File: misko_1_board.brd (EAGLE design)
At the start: 115 x 115 mm, 151 parts, among them IC1 ATMEGA1281-16AU, IC10 ORG1510-MK4, IC11 TPS3808G33DBVT, IC12 LTC4425, IC13 RN4678_BT_MODULE, IC14 ADXL345, IC15 74HCT1G32, IC16 FM25W256-SOIC, IC17 MICROSD_SPI_MODE, IC18 FH12-30S-0.5SH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

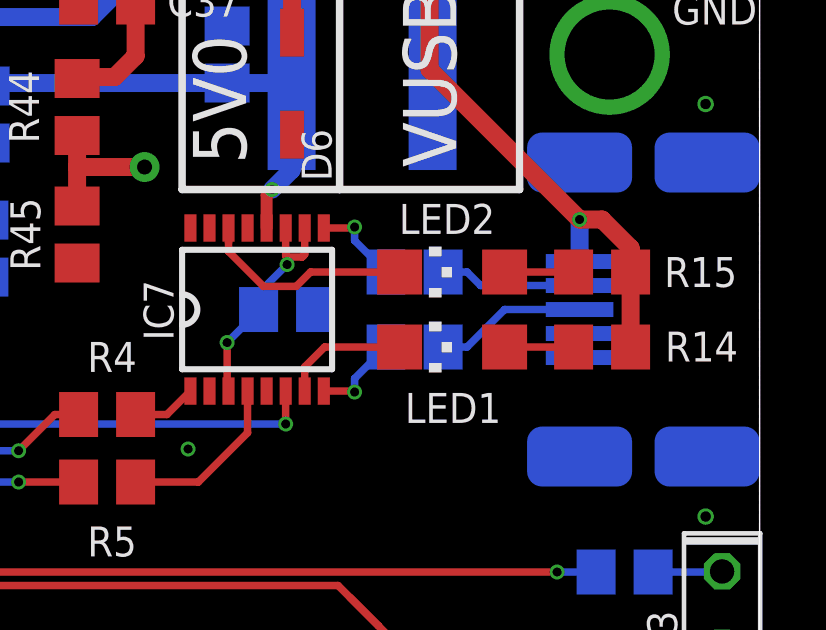
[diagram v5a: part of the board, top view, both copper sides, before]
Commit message: - named FTDI RX/TX LEDs properly in schematic and on board layout (tplace)
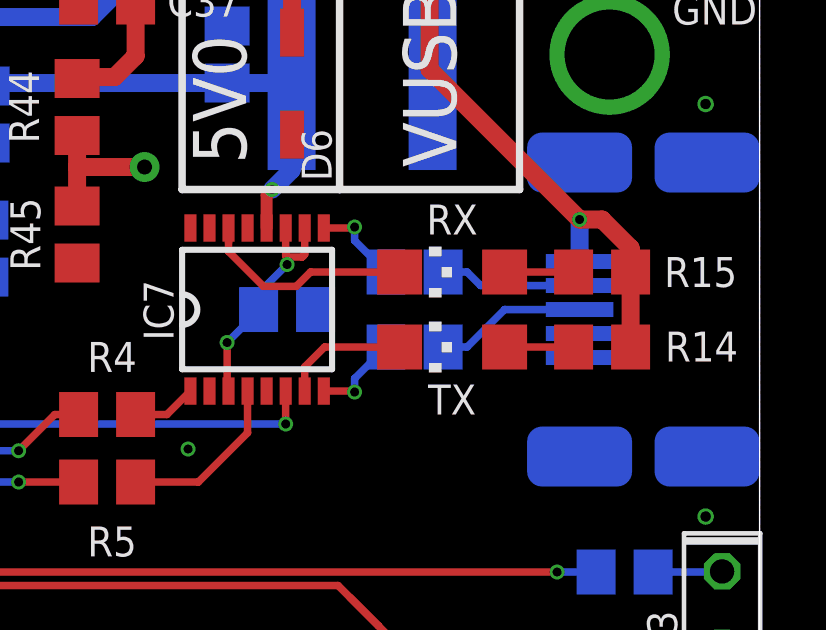
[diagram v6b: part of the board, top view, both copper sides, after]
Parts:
- LED1: value yellow -> TX
- LED2: value yellow -> RX
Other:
- board text added: "RX"
- board text added: "TX"
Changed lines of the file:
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@@
 <text x="97" y="66.5" size="1.778" layer="21" font="vector" rot="R90" align="center">5V0</text>
 <text x="93.5" y="61" size="1.778" layer="22" font="vector" rot="MR270" align="center">LiPo</text>
+<text x="104.75" y="62.5" size="1" layer="21" font="vector" align="center">RX</text>
+<text x="104.75" y="56.5" size="1" layer="21" font="vector" align="center">TX</text>
 </plain>
 <attributes>
@@
 <attribute name="VALUE" x="111.337" y="46.79" size="1.016" layer="27" ratio="10" rot="R270"/>
 </element>
-<element name="LED1" library="led" library_urn="urn:adsk.eagle:library:259" package="CHIPLED_1206" value="yellow" x="104.75" y="58.25" smashed="yes" rot="R90">
-<attribute name="NAME" x="104.78" y="56.22" size="1" layer="25" font="vector" align="center"/>
+<element name="LED1" library="led" library_urn="urn:adsk.eagle:library:259" package="CHIPLED_1206" value="TX" x="104.75" y="58.25" smashed="yes" rot="R90">
 <attribute name="VALUE" x="106.02" y="60.79" size="1.27" layer="27" rot="R180"/>
 </element>
-<element name="LED2" library="led" library_urn="urn:adsk.eagle:library:259" package="CHIPLED_1206" value="yellow" x="104.75" y="60.75" smashed="yes" rot="R90">
-<attribute name="NAME" x="104.58" y="62.52" size="1" layer="25" font="vector" align="center"/>
+<element name="LED2" library="led" library_urn="urn:adsk.eagle:library:259" package="CHIPLED_1206" value="RX" x="104.75" y="60.75" smashed="yes" rot="R90">
 <attribute name="VALUE" x="106.02" y="63.29" size="1.27" layer="27" rot="R180"/>
 </element>

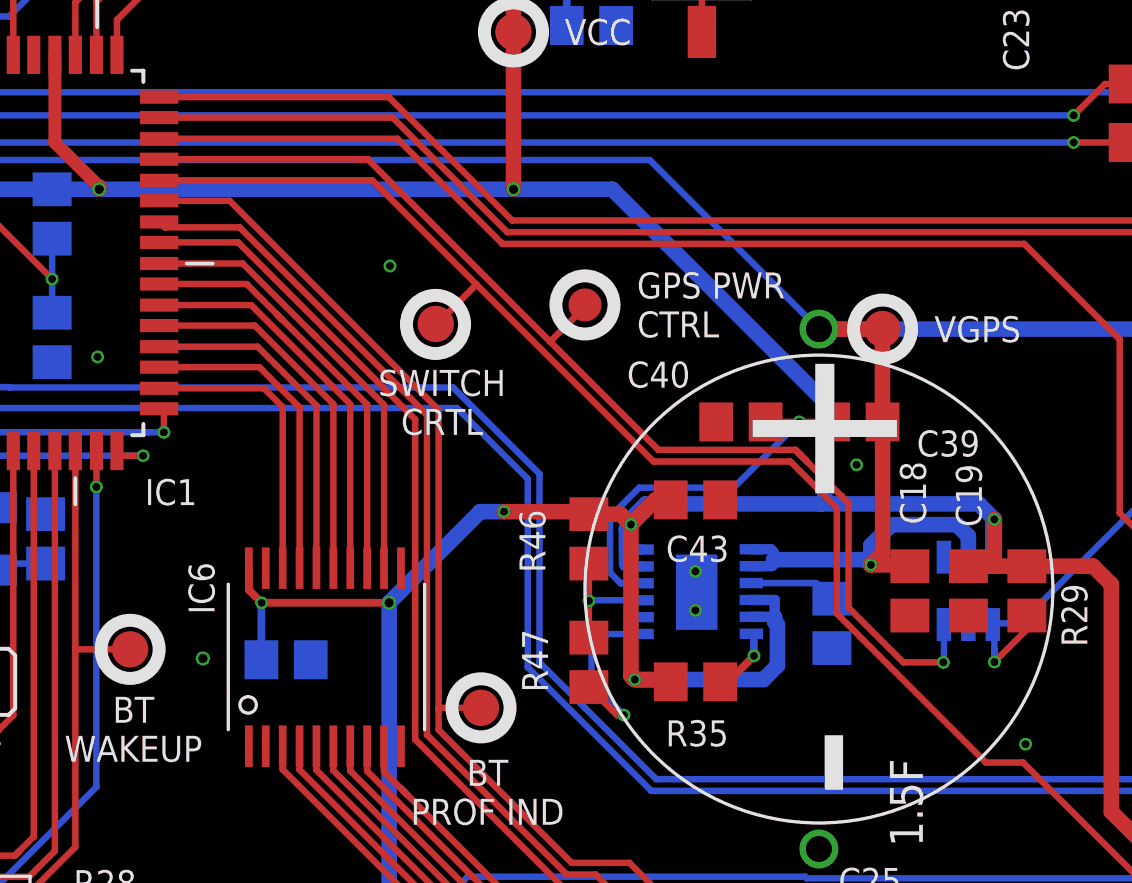
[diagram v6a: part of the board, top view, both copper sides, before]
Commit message: - added pulldown (R23) to GPS_POWER_CTL_PIN so that the receiver is turned off when micro controller resets
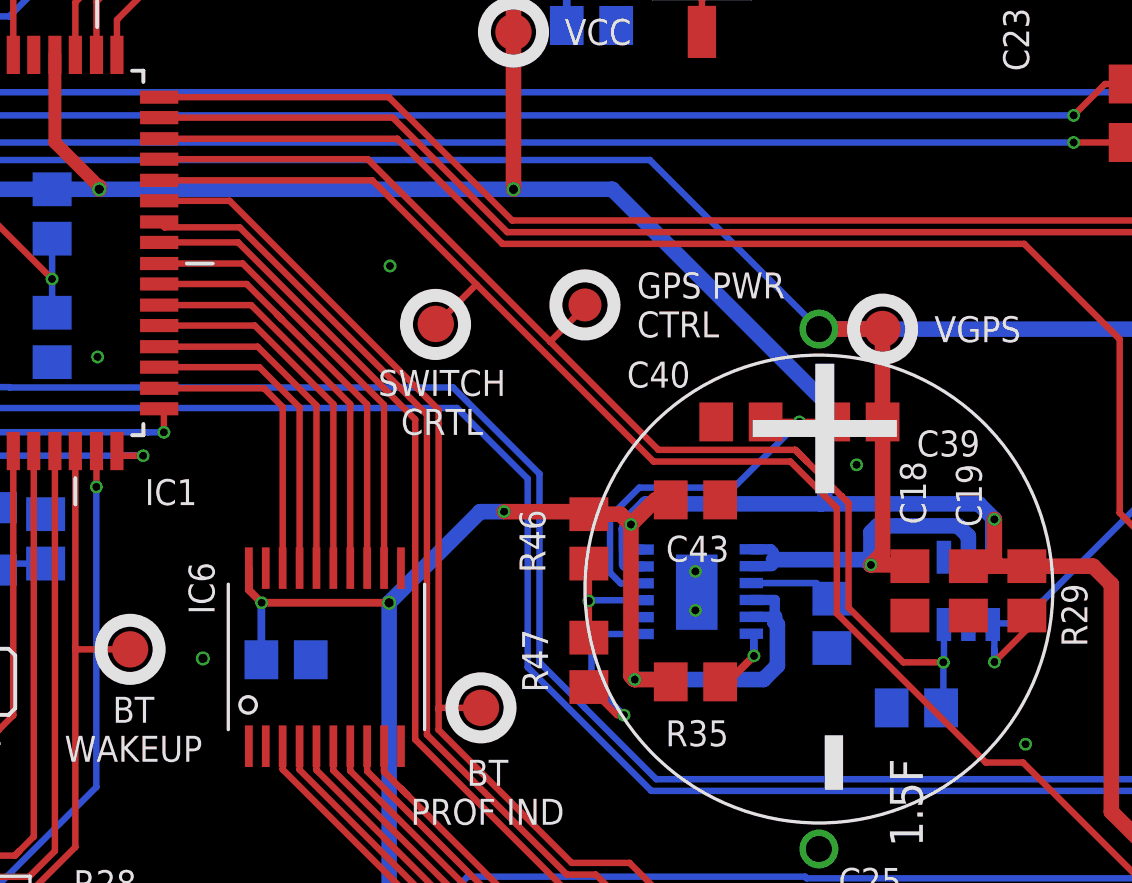
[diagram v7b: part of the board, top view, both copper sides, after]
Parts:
- added R23: 10k, resistor:R0805
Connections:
- net GND: now also R23.2
- net GPS_POWER_CTL_PIN: now also R23.1
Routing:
- net GPS_POWER_CTL_PIN: track 45.0 -> 46.4 mm
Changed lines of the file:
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@@
 <grid distance="0.25" unitdist="mm" unit="mm" style="lines" multiple="1" display="yes" altdistance="0.005" altunitdist="mm" altunit="mm"/>
 <layers>
-<layer number="1" name="Top" color="4" fill="1" visible="yes" active="yes"/>
+<layer number="1" name="Top" color="4" fill="1" visible="no" active="yes"/>
 <layer number="2" name="Route2" color="1" fill="3" visible="no" active="no"/>
 <layer number="3" name="Route3" color="4" fill="3" visible="no" active="no"/>
@@
 <layer number="14" name="Route14" color="1" fill="6" visible="no" active="no"/>
 <layer number="15" name="Route15" color="4" fill="6" visible="no" active="no"/>
-<layer number="16" name="Bottom" color="1" fill="1" visible="no" active="yes"/>
+<layer number="16" name="Bottom" color="1" fill="1" visible="yes" active="yes"/>
 <layer number="17" name="Pads" color="2" fill="1" visible="yes" active="yes"/>
 <layer number="18" name="Vias" color="2" fill="1" visible="yes" active="yes"/>
 <layer number="19" name="Unrouted" color="6" fill="1" visible="yes" active="yes"/>
 <layer number="20" name="Dimension" color="15" fill="1" visible="yes" active="yes"/>
-<layer number="21" name="tPlace" color="7" fill="1" visible="yes" active="yes"/>
-<layer number="22" name="bPlace" color="7" fill="1" visible="no" active="yes"/>
-<layer number="23" name="tOrigins" color="15" fill="1" visible="yes" active="yes"/>
-<layer number="24" name="bOrigins" color="15" fill="1" visible="no" active="yes"/>
-<layer number="25" name="tNames" color="7" fill="1" visible="yes" active="yes"/>
-<layer number="26" name="bNames" color="7" fill="1" visible="no" active="yes"/>
+<layer number="21" name="tPlace" color="7" fill="1" visible="no" active="yes"/>
+<layer number="22" name="bPlace" color="7" fill="1" visible="yes" active="yes"/>
+<layer number="23" name="tOrigins" color="15" fill="1" visible="no" active="yes"/>
+<layer number="24" name="bOrigins" color="15" fill="1" visible="yes" active="yes"/>
+<layer number="25" name="tNames" color="7" fill="1" visible="no" active="yes"/>
+<layer number="26" name="bNames" color="7" fill="1" visible="yes" active="yes"/>
 <layer number="27" name="tValues" color="7" fill="1" visible="no" active="yes"/>
 <layer number="28" name="bValues" color="7" fill="1" visible="no" active="yes"/>
@@
 <layer number="37" name="tTest" color="7" fill="1" visible="no" active="yes"/>
 <layer number="38" name="bTest" color="7" fill="1" visible="no" active="yes"/>
-<layer number="39" name="tKeepout" color="4" fill="11" visible="yes" active="yes"/>
-<layer number="40" name="bKeepout" color="1" fill="11" visible="no" active="yes"/>
-<layer number="41" name="tRestrict" color="4" fill="10" visible="yes" active="yes"/>
-<layer number="42" name="bRestrict" color="1" fill="10" visible="no" active="yes"/>
+<layer number="39" name="tKeepout" color="4" fill="11" visible="no" active="yes"/>
+<layer number="40" name="bKeepout" color="1" fill="11" visible="yes" active="yes"/>
+<layer number="41" name="tRestrict" color="4" fill="10" visible="no" active="yes"/>
+<layer number="42" name="bRestrict" color="1" fill="10" visible="yes" active="yes"/>
 <layer number="43" name="vRestrict" color="2" fill="10" visible="no" active="yes"/>
 <layer number="44" name="Drills" color="7" fill="1" visible="yes" active="yes"/>
@@
 <layer number="49" name="Reference" color="7" fill="1" visible="no" active="yes"/>
 <layer number="50" name="dxf" color="7" fill="1" visible="no" active="no"/>
-<layer number="51" name="tDocu" color="7" fill="1" visible="yes" active="yes"/>
-<layer number="52" name="bDocu" color="7" fill="1" visible="no" active="yes"/>
+<layer number="51" name="tDocu" color="7" fill="1" visible="no" active="yes"/>
+<layer number="52" name="bDocu" color="7" fill="1" visible="yes" active="yes"/>
 <layer number="53" name="tGND_GNDA" color="7" fill="9" visible="no" active="no"/>
 <layer number="54" name="bGND_GNDA" color="1" fill="9" visible="no" active="no"/>
@@
 <attribute name="NAME" x="57.5" y="66.5" size="1" layer="21" font="vector" rot="R180" align="center"/>
 </element>
+<element name="R23" library="resistor" library_urn="urn:adsk.eagle:library:348" package="R0805" value="10k" x="84.25" y="32" rot="MR0"/>
 </elements>
 <signals>
@@
 <contactref element="D6" pad="AN"/>
 <contactref element="D7" pad="AN"/>
+<contactref element="R23" pad="2"/>
 <wire x1="85.5" y1="67" x2="85.49" y2="67.01" width="0" layer="19" extent="16-16"/>
 <wire x1="32.25" y1="41" x2="31.5" y2="44.5" width="0" layer="19" extent="1-1"/>
@@
 <contactref element="TP8" pad="TP"/>
 <via x="85.29" y="33.75" extent="1-16" drill="0.3"/>
-<wire x1="85.3102" y1="35.2046" x2="85.3102" y2="33.7702" width="0.25" layer="16"/>
+<wire x1="85.3102" y1="33.7702" x2="85.3102" y2="35.2046" width="0.25" layer="16"/>
 <wire x1="85.3102" y1="33.7702" x2="85.29" y2="33.75" width="0.25" layer="16"/>
 <wire x1="81.37588125" y1="40.1394875" x2="81.6394875" y2="39.87588125" width="0.25" layer="1"/>
@@
 <wire x1="85.29" y1="33.75" x2="83.745371875" y2="33.75" width="0.25" layer="1"/>
 <contactref element="IC1" pad="45"/>
-<wire x1="55.12" y1="53.1068" x2="62.75" y2="53.1068" width="0.25" layer="1"/>
-<wire x1="62.75" y1="53.1068" x2="63.1432" y2="53.1068" width="0.25" layer="1"/>
+<wire x1="55.12" y1="53.1068" x2="63.1432125" y2="53.1068" width="0.25" layer="1"/>
 <wire x1="71.5" y1="47.5" x2="71.5" y2="47.4283" width="0.25" layer="1"/>
 <wire x1="71.5" y1="47.4283" x2="70.16085625" y2="46.08915625" width="0.25" layer="1"/>
-<wire x1="62.75" y1="53.1068" x2="63.1432125" y2="53.1068" width="0.25" layer="1"/>
 <wire x1="63.1432125" y1="53.1068" x2="70.16085625" y2="46.08915625" width="0.25" layer="1"/>
 <wire x1="70.16085625" y1="46.08915625" x2="74.3250125" y2="41.925" width="0.25" layer="1"/>
@@
 <wire x1="74.3250125" y1="41.925" x2="79.59035625" y2="41.925" width="0.25" layer="1"/>
 <wire x1="79.59035625" y1="41.925" x2="80.023075" y2="41.49228125" width="0.25" layer="1"/>
+<contactref element="R23" pad="1"/>
+<wire x1="85.29" y1="33.75" x2="85.29" y2="32.09" width="0.25" layer="16"/>
+<wire x1="85.29" y1="32.09" x2="85.2" y2="32" width="0.25" layer="16"/>
 </signal>
 <signal name="PDI_UART0_CTS_PIN" class="3">
@@
 <wire x1="78.75" y1="37.5" x2="78.75" y2="37.7" width="0.4" layer="16"/>
 <wire x1="78.75" y1="37.7" x2="78.75" y2="38" width="0.4" layer="16"/>
-<wire x1="86.25" y1="37.7954" x2="86.25" y2="38.60321875" width="0.6" layer="16"/>
-<wire x1="86.25" y1="38.60321875" x2="85.80641875" y2="39.0468" width="0.6" layer="16"/>
-<wire x1="85.80641875" y1="39.0468" x2="83.2968" y2="39.0468" width="0.6" layer="16"/>
-<wire x1="82.5" y1="38.25" x2="83.2968" y2="39.0468" width="0.6" layer="16"/>
+<wire x1="86.25" y1="38.60321875" x2="86.25" y2="37.7954" width="0.6" layer="16"/>
 <wire x1="37.5" y1="52.5" x2="37.5" y2="55.6" width="0.25" layer="16"/>
 <wire x1="37.5" y1="55.6" x2="37.7" y2="55.8" width="0.25" layer="16"/>
@@
 <wire x1="78.75" y1="37.7" x2="82.3" y2="37.7" width="0.6" layer="16"/>
 <wire x1="82.3" y1="37.7" x2="82.5" y2="37.5" width="0.6" layer="16"/>
-<wire x1="82.5" y1="37.5" x2="82.5" y2="38.25" width="0.6" layer="16"/>
 <wire x1="97.23" y1="41.418265625" x2="97.25" y2="41.438265625" width="0.6" layer="1"/>
 <wire x1="97.25" y1="41.438265625" x2="97.25" y2="43.5" width="0.6" layer="1"/>
@@
 <wire x1="80.5" y1="46.57" x2="73.995" y2="53.075" width="0.25" layer="16"/>
 <wire x1="73.995" y1="53.075" x2="42.27138125" y2="53.075" width="0.25" layer="16"/>
+<wire x1="82.5" y1="37.5" x2="82.5" y2="38.75" width="0.6" layer="16"/>
+<wire x1="82.5" y1="38.75" x2="82.75" y2="39" width="0.6" layer="16"/>
+<wire x1="82.75" y1="39" x2="85.85321875" y2="39" width="0.6" layer="16"/>
+<wire x1="85.85321875" y1="39" x2="86.25" y2="38.60321875" width="0.6" layer="16"/>
 </signal>
 <signal name="PFI" class="2">
